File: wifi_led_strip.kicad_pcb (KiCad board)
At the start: 2 copper layers, 88.4 x 17.8 mm, 14 parts, among them J1 Serial, J2 Power, J3 ESP01, J4 Leds, SW1 Flash, SW2 Reset, U1 TLV1117-33

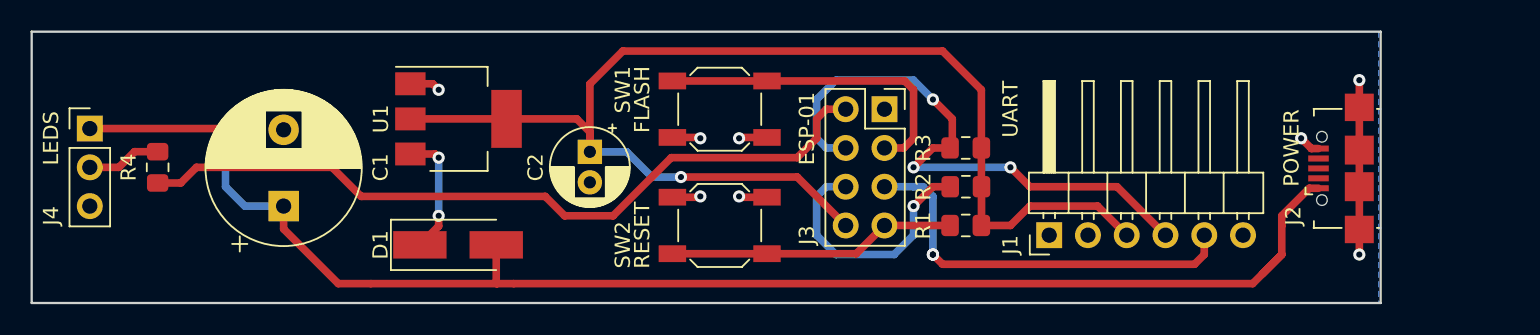
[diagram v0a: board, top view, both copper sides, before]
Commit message: Add names and generate image
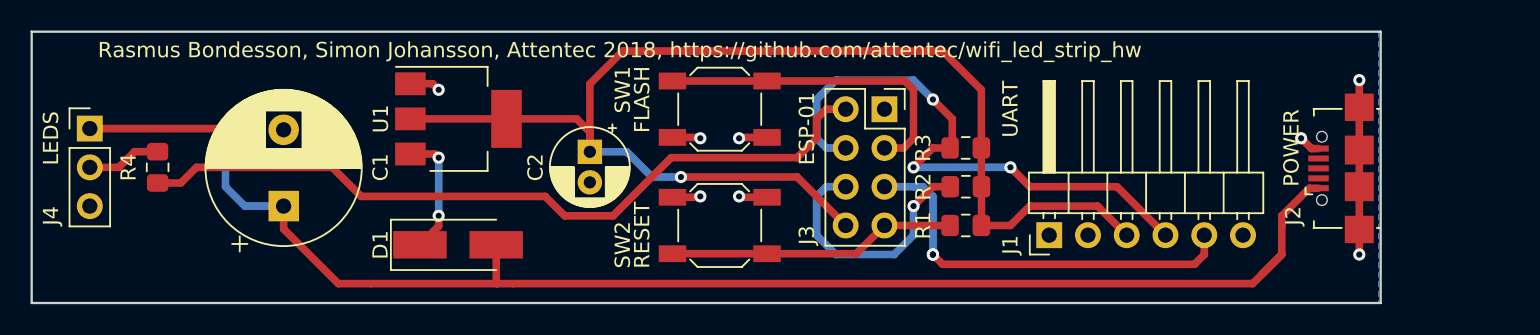
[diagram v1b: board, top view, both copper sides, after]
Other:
- board text added: "Rasmus Bondesson, Simon Johansson, Attentec 2018, https://github.com/attentec/wifi_led_strip_hw"
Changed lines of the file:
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@@
-(kicad_pcb (version 20171130) (host pcbnew 5.0.0-fee4fd1~66~ubuntu16.04.1)
+(kicad_pcb (version 20171130) (host pcbnew 5.0.1-33cea8e~68~ubuntu14.04.1)
   (general
     (thickness 1.6)
-    (drawings 10)
+    (drawings 11)
     (tracks 138)
     (zones 0)
@@
     (pad_drill 0.762)
     (pad_to_mask_clearance 0.2)
+    (solder_mask_min_width 0.25)
     (aux_axis_origin 0 0)
     (visible_elements FFFFFF7F)
@@
     )
   )
+  (gr_text "Rasmus Bondesson, Simon Johansson, Attentec 2018, https://github.com/attentec/wifi_led_strip_hw" (at 118 99) (layer F.SilkS)
+    (effects (font (size 1 1) (thickness 0.15)) (justify left))
+  )
   (gr_text LEDS (at 114.935 104.775 90) (layer F.SilkS)
